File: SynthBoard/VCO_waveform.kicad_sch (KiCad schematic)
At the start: 26 parts, among them IC6 AS321KTR-E1, IC7 4013, J1 Output, J2 Input, Q18 Q_NPN_ECB

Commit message: SynthBoard
部品をSMDにしてVCO+LFOを配置した
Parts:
- removed J2: Input, Connector_PinSocket_2.54mm:PinSocket_2x05_P2.54mm_Vertical, symbol Connector_Generic:Conn_02x05_Odd_Even
- removed Q18: Q_NPN_ECB, Package_TO_SOT_THT:TO-92_HandSolder, symbol Transistor_BJT:Q_NPN_ECB
- added Q1: 2SC1623(RANGE:300-400), SamacSys_parts:SOT95P237X125-3N, symbol SamacSys_Parts:2SC1623-A
- C54: value 10uF/16VBP -> CL21A106KAYNNNE; footprint Capacitor_THT:C_Radial_D6.3mm_H7.0mm_P2.50mm -> Capacitor_SMD:C_0805_2012Metric_Pad1.18x1.45mm_HandSolder
- IC6: value AS321KTR-E1 -> AS321KTR-G1
- IC7: value 4013 -> HEF4013BT,653
- R186, R187, R188, R25: footprint Resistor_THT:R_Axial_DIN0207_L6.3mm_D2.5mm_P2.54mm_Vertical -> Resistor_THT:R_Axial_DIN0207_L6.3mm_D2.5mm_P7.62mm_Horizontal
- R19: value 47K -> 0805W8F4702T5E; footprint Resistor_THT:R_Axial_DIN0207_L6.3mm_D2.5mm_P2.54mm_Vertical -> Resistor_SMD:R_0805_2012Metric_Pad1.20x1.40mm_HandSolder
- R20, R21: value 47k -> 0805W8F4702T5E; footprint Resistor_THT:R_Axial_DIN0207_L6.3mm_D2.5mm_P2.54mm_Vertical -> Resistor_SMD:R_0805_2012Metric_Pad1.20x1.40mm_HandSolder
- R22: value 10K -> 0805W8F1002T5E; footprint Resistor_THT:R_Axial_DIN0207_L6.3mm_D2.5mm_P2.54mm_Vertical -> Resistor_SMD:R_0805_2012Metric_Pad1.20x1.40mm_HandSolder
- R23: value 1K -> 0805W8F1001T5E; footprint Resistor_THT:R_Axial_DIN0207_L6.3mm_D2.5mm_P2.54mm_Vertical -> Resistor_SMD:R_0805_2012Metric_Pad1.20x1.40mm_HandSolder
- R24: value 68K -> 0805W8F6802T5E; footprint Resistor_THT:R_Axial_DIN0207_L6.3mm_D2.5mm_P2.54mm_Vertical -> Resistor_SMD:R_0805_2012Metric_Pad1.20x1.40mm_HandSolder
- R258: value 470k -> 0805w8f4703t5e; footprint Resistor_THT:R_Axial_DIN0207_L6.3mm_D2.5mm_P2.54mm_Vertical -> Resistor_SMD:R_0805_2012Metric_Pad1.20x1.40mm_HandSolder
- R259: value 33K -> 0805W8F3302T5E; footprint Resistor_THT:R_Axial_DIN0207_L6.3mm_D2.5mm_P2.54mm_Vertical -> Resistor_SMD:R_0805_2012Metric_Pad1.20x1.40mm_HandSolder
- S1: footprint MS2301L6 -> SamacSys_parts:MS2301L6
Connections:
- net GNDA: now also Q1.2 (E)
- net VPseparate: now also Q1.3 (C)
- net at R22.2, R23.2: now also Q1.1 (B)
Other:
- note added: "10K"
- note added: "10uF"
- note added: "1K"
- note added: "33K"
- note added: "470K"
- note added: "47K"
- note added: "68K"
- moved on the sheet: R22, R23, R24

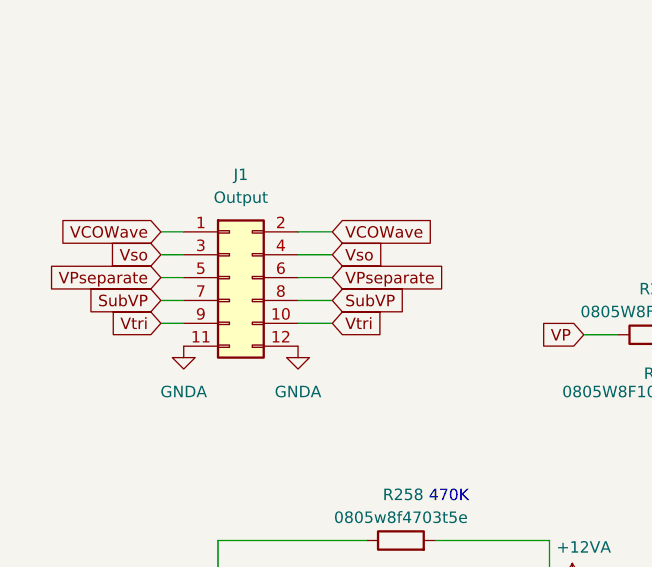
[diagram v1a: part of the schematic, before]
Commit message: SynthBorad
デジタルも配置した
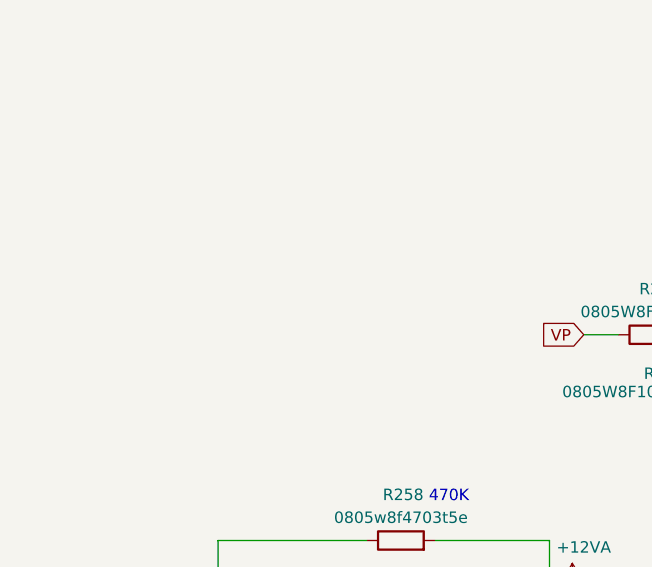
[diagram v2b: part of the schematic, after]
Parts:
- removed J1: Output, Connector_PinSocket_2.54mm:PinSocket_2x06_P2.54mm_Vertical, symbol Connector_Generic:Conn_02x06_Odd_Even
